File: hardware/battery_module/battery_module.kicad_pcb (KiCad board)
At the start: 2 copper layers, 0 parts

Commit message: Placed all parts and added edge routes from template.
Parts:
- added BT1: BATTERY, _CrumpPrints:CR2032_HOLDER, F.Cu at (148.5, 105.0)
- added SW1: SPST, _CrumpPrints:SPDT_slide_switch, F.Cu at (148.5, 124.5)
- added U1: SnapStack, _CrumpPrints:SnapStack, F.Cu at (148.5, 105.0)
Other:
- board outline added: 50 x 50 mm

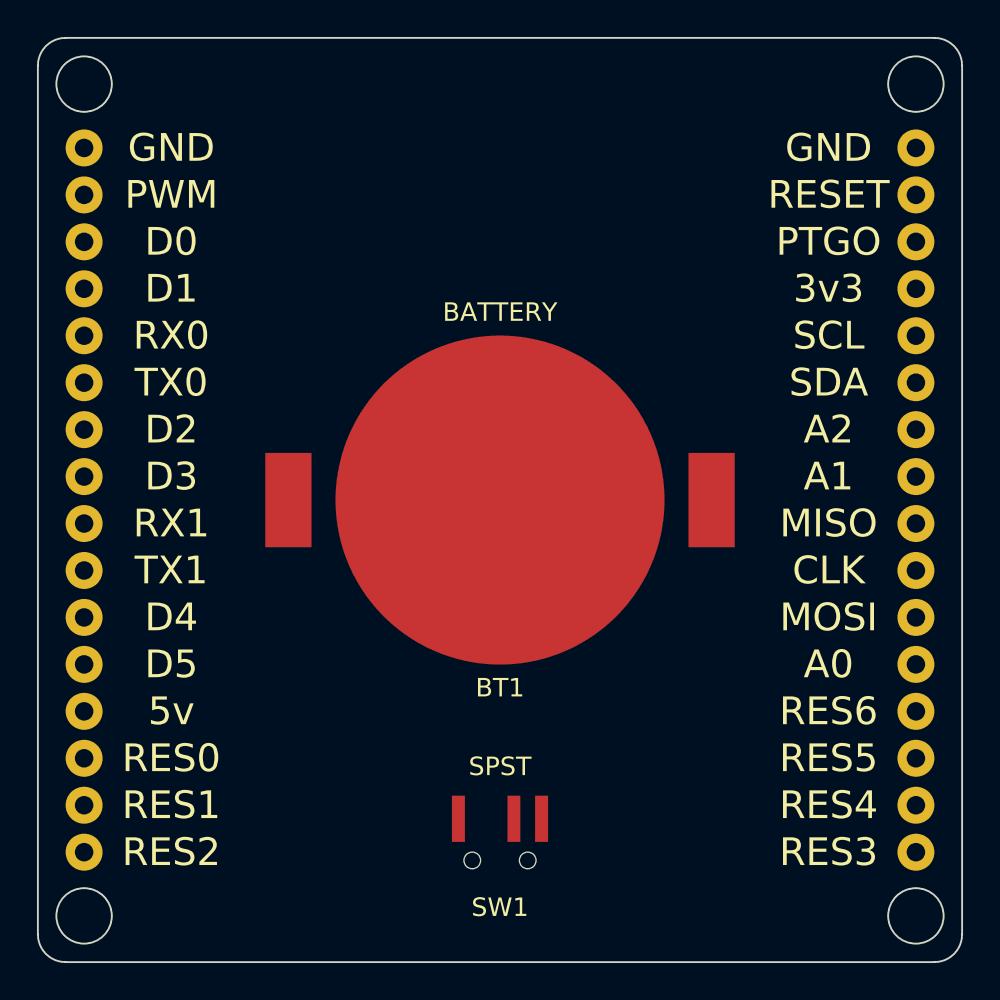
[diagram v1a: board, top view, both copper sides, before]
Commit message: Finished battery board layout.
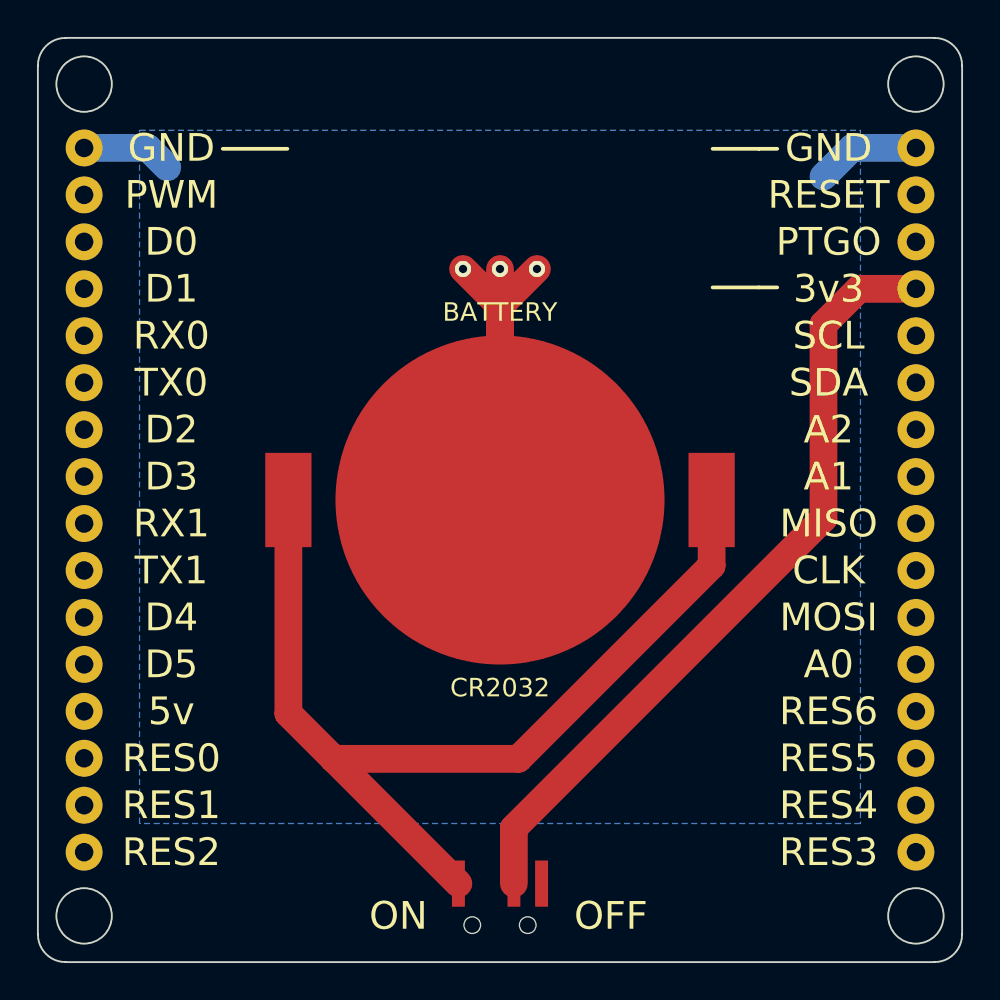
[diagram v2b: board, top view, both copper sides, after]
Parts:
- moved SW1 3.50 mm to (148.5, 128.0)
- renumbered BT1 to CR2032
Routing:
- net Net-(BT1-Pad1): track 0.00 -> 52.9 mm
- net Net-(SW1-Pad2): track 0.00 -> 43.0 mm
- net Net-(BT1-Pad2): track 0.00 -> 39.2 mm, vias 0 -> 3
- added copper zone on B.Cu, net Net-(BT1-Pad2)
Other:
- net class POWER added: clearance 0.254, trace_width 1.5, via_dia 0.889, via_drill 0.635
- board text added: "OFF"
- board text added: "ON"
- board text added: "SnapStack Battery Board CR2032 v0.1"
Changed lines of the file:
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@@
   (general
     (links 5)
-    (no_connects 5)
-    (area 124.7471 84.6996 172.2551 128.069)
+    (no_connects 0)
+    (area 123.449999 79.949999 173.550001 130.050001)
     (thickness 1.6)
-    (drawings 0)
-    (tracks 0)
+    (drawings 25)
+    (tracks 22)
     (zones 0)
     (modules 3)
@@
   (page A4)
   (layers
-    (0 F.Cu signal)
-    (31 B.Cu signal)
+    (0 F.Cu signal hide)
+    (31 B.Cu signal hide)
     (32 B.Adhes user)
     (33 F.Adhes user)
@@
     (uvia_dia 0.508)
     (uvia_drill 0.127)
+  )
+  (net_class POWER ""
+    (clearance 0.254)
+    (trace_width 1.5)
+    (via_dia 0.889)
+    (via_drill 0.635)
+    (uvia_dia 0.508)
+    (uvia_drill 0.127)
     (add_net "Net-(BT1-Pad1)")
     (add_net "Net-(BT1-Pad2)")
@@
     (add_net "Net-(U1-Pad8)")
     (add_net "Net-(U1-Pad9)")
-  )
-  (module _CrumpPrints:CR2032_HOLDER (layer F.Cu)
-    (at 148.5011 105.0036)
-    (descr http://www.mouser.com/ds/2/238/bat-hld-001-220194.pdf)
-    (tags "Linx Battery Holder 2032 bat-hld-001")
-    (fp_text reference BT1 (at 0 10.16) (layer F.SilkS)
-      (effects (font (size 1 1) (thickness 0.15)))
-    )
-    (fp_text value BATTERY (at 0 -10.16) (layer F.SilkS)
-      (effects (font (size 1 1) (thickness 0.15)))
-    )
-    (pad 1 smd rect (at -11.45 0) (size 2.5 5.1) (layers F.Cu F.Paste F.Mask)
-      (net 1 "Net-(BT1-Pad1)"))
-    (pad 1 smd rect (at 11.45 0) (size 2.5 5.1) (layers F.Cu F.Paste F.Mask)
-      (net 1 "Net-(BT1-Pad1)"))
-    (pad 2 smd circle (at 0 0) (size 17.8 17.8) (layers F.Cu F.Paste F.Mask)
-      (net 2 "Net-(BT1-Pad2)"))
   )
   (module _CrumpPrints:SnapStack (layer F.Cu)
@@
       (net 32 "Net-(U1-Pad17)"))
   )
+  (module _CrumpPrints:CR2032_HOLDER (layer F.Cu)
+    (at 148.5 105)
+    (descr http://www.mouser.com/ds/2/238/bat-hld-001-220194.pdf)
+    (tags "Linx Battery Holder 2032 bat-hld-001")
+    (fp_text reference CR2032 (at 0 10.16) (layer F.SilkS)
+      (effects (font (size 1 1) (thickness 0.15)))
+    )
+    (fp_text value BATTERY (at 0 -10.16) (layer F.SilkS)
+      (effects (font (size 1 1) (thickness 0.15)))
+    )
+    (pad 1 smd rect (at -11.45 0) (size 2.5 5.1) (layers F.Cu F.Paste F.Mask)
+      (net 1 "Net-(BT1-Pad1)"))
+    (pad 1 smd rect (at 11.45 0) (size 2.5 5.1) (layers F.Cu F.Paste F.Mask)
+      (net 1 "Net-(BT1-Pad1)"))
+    (pad 2 smd circle (at 0 0) (size 17.8 17.8) (layers F.Cu F.Paste F.Mask)
+      (net 2 "Net-(BT1-Pad2)"))
+  )
   (module _CrumpPrints:SPDT_slide_switch (layer F.Cu)
-    (at 148.5 124.5)
+    (at 148.5 128)
     (descr http://www.alps.com/prod/info/E/HTML/Switch/Slide/SSSS8/SSSS810701.html)
     (tags "SPDT, slide, switch, alps, ssss810701")
-    (fp_text reference SW1 (at 0 2.54) (layer F.SilkS)
+    (fp_text reference SW1 (at 0 2.54) (layer F.SilkS) hide
       (effects (font (size 1 1) (thickness 0.15)))
     )
-    (fp_text value SPST (at 0 -5.08) (layer F.SilkS)
+    (fp_text value SPST (at 0 -5.08) (layer F.SilkS) hide
       (effects (font (size 1 1) (thickness 0.15)))
     )
@@
       (net 20 "Net-(SW1-Pad2)"))
     (pad 3 smd rect (at 2.25 -2.25) (size 0.7 2.5) (layers F.Cu F.Paste F.Mask))
+  )
+  (gr_line (start 160 93.5) (end 163.5 93.5) (angle 90) (layer B.SilkS) (width 0.2))
+  (gr_line (start 160 86) (end 163.5 86) (angle 90) (layer B.SilkS) (width 0.2))
+  (gr_line (start 133.5 86) (end 137 86) (angle 90) (layer B.SilkS) (width 0.2))
+  (gr_line (start 137 86) (end 133.5 86) (angle 90) (layer F.SilkS) (width 0.2))
+  (gr_line (start 162.5 93.5) (end 160 93.5) (angle 90) (layer F.SilkS) (width 0.2))
+  (gr_line (start 162.5 86) (end 160 86) (angle 90) (layer F.SilkS) (width 0.2))
+  (gr_line (start 163.5 93.5) (end 162.5 93.5) (angle 90) (layer F.SilkS) (width 0.2))
+  (gr_line (start 163.5 86) (end 162.5 86) (angle 90) (layer F.SilkS) (width 0.2))
+  (gr_text "SnapStack\nBattery Board\nCR2032\nv0.1" (at 148.5 105) (layer B.SilkS)
+    (effects (font (size 1.5 1.5) (thickness 0.3)) (justify mirror))
+  )
+  (gr_text ON (at 143 127.5) (layer F.SilkS)
+    (effects (font (size 1.5 1.5) (thickness 0.3)))
+  )
+  (gr_text OFF (at 154.5 127.5) (layer B.SilkS)
+    (effects (font (size 1.5 1.5) (thickness 0.3)) (justify mirror))
+  )
+  (gr_text OFF (at 154.5 127.5) (layer F.SilkS)
+    (effects (font (size 1.5 1.5) (thickness 0.3)))
+  )
+  (gr_text ON (at 143 127.5) (layer B.SilkS)
+    (effects (font (size 1.5 1.5) (thickness 0.3)) (justify mirror))
   )
   (gr_circle (center 171 127.5) (end 171 129) (layer Edge.Cuts) (width 0.1))
@@
   (gr_arc (start 172 81.5) (end 172 80) (angle 90) (layer Edge.Cuts) (width 0.1))
   (gr_arc (start 125 81.5) (end 123.5 81.5) (angle 90) (layer Edge.Cuts) (width 0.1))
+  (segment (start 159.95 105) (end 159.95 108.55) (width 1.5) (layer F.Cu) (net 1))
+  (segment (start 149.5 119) (end 139.5 119) (width 1.5) (layer F.Cu) (net 1))
+  (segment (start 159.95 108.55) (end 149.5 119) (width 1.5) (layer F.Cu) (net 1))
+  (segment (start 137.05 105) (end 137.05 116.55) (width 1.5) (layer F.Cu) (net 1))
+  (segment (start 137.05 116.55) (end 139.5 119) (width 1.5) (layer F.Cu) (net 1))
+  (segment (start 139.5 119) (end 146.25 125.75) (width 1.5) (layer F.Cu) (net 1))
+  (segment (start 171.0011 85.9536) (end 167.5464 85.9536) (width 1.5) (layer B.Cu) (net 2))
+  (segment (start 167.5464 85.9536) (end 166 87.5) (width 1.5) (layer B.Cu) (net 2))
+  (segment (start 126.0011 85.9536) (end 129.4536 85.9536) (width 1.5) (layer B.Cu) (net 2))
+  (segment (start 129.4536 85.9536) (end 130.5 87) (width 1.5) (layer B.Cu) (net 2))
+  (segment (start 148.5 94.5) (end 146.5 92.5) (width 1.5) (layer F.Cu) (net 2))
+  (via (at 146.5 92.5) (size 0.889) (layers F.Cu B.Cu) (net 2))
+  (segment (start 148.5 105) (end 148.5 94.5) (width 1.5) (layer F.Cu) (net 2))
+  (via (at 150.5 92.5) (size 0.889) (layers F.Cu B.Cu) (net 2))
+  (segment (start 148.5 94.5) (end 150.5 92.5) (width 1.5) (layer F.Cu) (net 2))
+  (segment (start 148.5 105) (end 148.5 92.5) (width 1.5) (layer F.Cu) (net 2))
+  (via (at 148.5 92.5) (size 0.889) (layers F.Cu B.Cu) (net 2))
+  (segment (start 149.25 125.75) (end 149.25 122.75) (width 1.5) (layer F.Cu) (net 20))
+  (segment (start 167.9264 93.5736) (end 171.0011 93.5736) (width 1.5) (layer F.Cu) (net 20))
+  (segment (start 166 95.5) (end 167.9264 93.5736) (width 1.5) (layer F.Cu) (net 20))
+  (segment (start 166 106) (end 166 95.5) (width 1.5) (layer F.Cu) (net 20))
+  (segment (start 149.25 122.75) (end 166 106) (width 1.5) (layer F.Cu) (net 20))
+  (zone (net 2) (net_name "Net-(BT1-Pad2)") (layer B.Cu) (hatch edge 0.508)
+    (connect_pads (clearance 0.508))
+    (min_thickness 0.254)
+    (fill yes (arc_segments 16) (thermal_gap 0.508) (thermal_bridge_width 0.508))
+    (polygon
+      (pts
+        (xy 168 122.5) (xy 129 122.5) (xy 129 85) (xy 168 85)
+      )
+    )
+  )
 )
